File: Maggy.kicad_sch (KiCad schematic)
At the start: 75 parts, among them CN1 0430450800, CN2 430451000, J1 XY308-2.54-2P, J2 XY308-2.54-2P, J3 XY308-2.54-2P, J4 XY308-2.54-2P, U1 CH224K, U10 INA214AIDCKR, U11 Socket for Teensy 4.1 (2x 1x2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, U12 INA214AIDCKR, U13 INA214AIDCKR, U14 TMAG5170A2DGKR, U15 TMAG5170A2DGKR, U16 TMAG5170A2DGKR, U17 TMAG5170A2DGKR, U18 TMAG5170A2DGKR, U2 A4950ELJTR-T, U3 A4950ELJTR-T, U4 A4950ELJTR-T, U5 A4950ELJTR-T, U6 TLV2372, U7 LM1117S-3.3, U8 LM1117S-5.0, U9 INA214AIDCKR

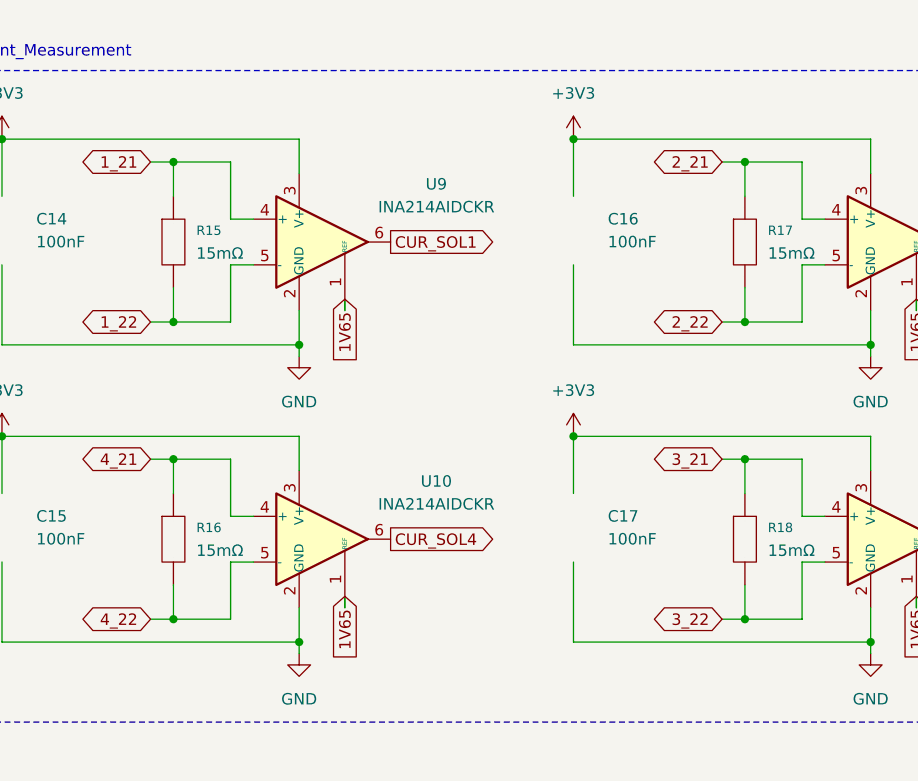
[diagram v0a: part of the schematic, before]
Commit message: chore: replace current sensing resistors' symbols from EasyEDA to KiCad ones
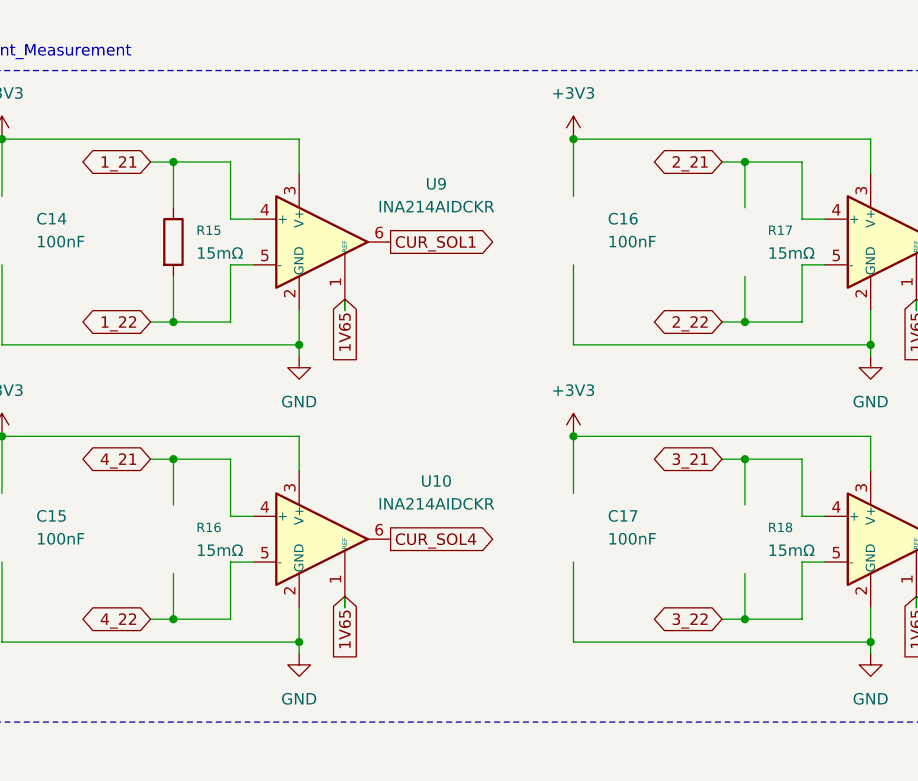
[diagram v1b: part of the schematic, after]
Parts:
- R15, R16, R17, R18: symbol ProPrj_Mag-easyedapro:1206W3F100MT5E -> Device:R
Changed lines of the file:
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@@
 	(wire
 		(pts
+			(xy 224.79 240.03) (xy 224.79 245.11)
+		)
+		(stroke
+			(width 0)
+			(type default)
+		)
+	)
+	(wire
+		(pts
 			(xy 130.81 133.35) (xy 124.46 133.35)
 		)
@@
 	(wire
 		(pts
-			(xy 288.29 241.3) (xy 288.29 245.11)
+			(xy 288.29 240.03) (xy 288.29 245.11)
 		)
 		(stroke
@@
 	(wire
 		(pts
-			(xy 288.29 260.35) (xy 288.29 264.16)
-		)
-		(stroke
-			(width 0)
-			(type default)
-		)
-	)
-	(wire
-		(pts
 			(xy 137.16 121.92) (xy 137.16 124.46)
 		)
@@
 	(wire
 		(pts
-			(xy 224.79 241.3) (xy 224.79 245.11)
-		)
-		(stroke
-			(width 0)
-			(type default)
-		)
-	)
-	(wire
-		(pts
 			(xy 125.73 48.26) (xy 139.7 48.26)
 		)
@@
 	(wire
 		(pts
-			(xy 288.29 274.32) (xy 288.29 278.13)
+			(xy 288.29 273.05) (xy 288.29 278.13)
 		)
 		(stroke
@@
 	(wire
 		(pts
-			(xy 224.79 227.33) (xy 224.79 231.14)
+			(xy 224.79 227.33) (xy 224.79 232.41)
 		)
 		(stroke
@@
 	(wire
 		(pts
-			(xy 288.29 227.33) (xy 288.29 231.14)
+			(xy 288.29 227.33) (xy 288.29 232.41)
 		)
 		(stroke
@@
 	(wire
 		(pts
+			(xy 288.29 260.35) (xy 288.29 265.43)
+		)
+		(stroke
+			(width 0)
+			(type default)
+		)
+	)
+	(wire
+		(pts
 			(xy 78.74 219.71) (xy 85.09 219.71)
 		)
@@
 	(wire
 		(pts
+			(xy 224.79 260.35) (xy 224.79 265.43)
+		)
+		(stroke
+			(width 0)
+			(type default)
+		)
+	)
+	(wire
+		(pts
 			(xy 307.34 243.84) (xy 307.34 242.57)
 		)
@@
 	(wire
 		(pts
-			(xy 224.79 274.32) (xy 224.79 278.13)
+			(xy 224.79 273.05) (xy 224.79 278.13)
 		)
 		(stroke
@@
 	(wire
 		(pts
-			(xy 224.79 260.35) (xy 224.79 264.16)
-		)
-		(stroke
-			(width 0)
-			(type default)
-		)
-	)
-	(wire
-		(pts
 			(xy 85.09 240.03) (xy 85.09 242.57)
 		)
@@
 	)
 	(symbol
-		(lib_id "ProPrj_Mag-easyedapro:1206W3F100MT5E")
-		(at 224.79 269.24 270)
+		(lib_id "Device:R")
+		(at 224.79 269.24 0)
 		(unit 1)
 		(body_style 0)
@@
 		(fields_autoplaced yes)
 		(property "Reference" "R16"
-			(at 227.33 267.97 90)
+			(at 227.33 267.97 0)
 			(show_name no)
 			(do_not_autoplace no)
@@
 		)
 		(property "Value" "15mΩ"
-			(at 227.33 270.5099 90)
+			(at 227.33 270.5099 0)
 			(show_name no)
 			(do_not_autoplace no)
@@
 		)
 		(property "Footprint" "Resistor_SMD:R_1206_3216Metric"
-			(at 224.79 269.24 0)
+			(at 223.012 269.24 90)
 			(hide yes)
 			(show_name no)
@@
 			)
 		)
-		(property "Description" "Type:Thick Film Resistors Resistance:10mΩ Tolerance:±1% Tolerance:±1% Power(Watts): Overload Voltage (Max): Temperature Coefficient:- Temperature Coefficient:- Operating Temperature Range:-55°C~+155°C Operating Temperature Range:-55°C~+155°C"
+		(property "Description" "Resistor"
 			(at 224.79 269.24 0)
 			(hide yes)
@@
 	)
 	(symbol
-		(lib_id "ProPrj_Mag-easyedapro:1206W3F100MT5E")
-		(at 288.29 269.24 270)
+		(lib_id "Device:R")
+		(at 288.29 269.24 0)
 		(unit 1)
 		(body_style 0)
@@
 		(fields_autoplaced yes)
 		(property "Reference" "R18"
-			(at 290.83 267.97 90)
+			(at 290.83 267.97 0)
 			(show_name no)
 			(do_not_autoplace no)
@@
 		)
 		(property "Value" "15mΩ"
-			(at 290.83 270.5099 90)
+			(at 290.83 270.5099 0)
 			(show_name no)
 			(do_not_autoplace no)
@@
 		)
 		(property "Footprint" "Resistor_SMD:R_1206_3216Metric"
-			(at 288.29 269.24 0)
+			(at 286.512 269.24 90)
 			(hide yes)
 			(show_name no)
@@
 			)
 		)
-		(property "Description" "Type:Thick Film Resistors Resistance:10mΩ Tolerance:±1% Tolerance:±1% Power(Watts): Overload Voltage (Max): Temperature Coefficient:- Temperature Coefficient:- Operating Temperature Range:-55°C~+155°C Operating Temperature Range:-55°C~+155°C"
+		(property "Description" "Resistor"
 			(at 288.29 269.24 0)
 			(hide yes)
@@
 	)
 	(symbol
-		(lib_id "ProPrj_Mag-easyedapro:1206W3F100MT5E")
-		(at 224.79 236.22 270)
+		(lib_id "Device:R")
+		(at 224.79 236.22 0)
 		(unit 1)
-		(body_style 0)
+		(body_style 1)
 		(exclude_from_sim no)
 		(in_bom yes)
@@
 		(fields_autoplaced yes)
 		(property "Reference" "R15"
-			(at 227.33 234.95 90)
+			(at 227.33 234.95 0)
 			(show_name no)
 			(do_not_autoplace no)
@@
 		)
 		(property "Value" "15mΩ"
-			(at 227.33 237.4899 90)
+			(at 227.33 237.4899 0)
 			(show_name no)
 			(do_not_autoplace no)
@@
 		)
 		(property "Footprint" "Resistor_SMD:R_1206_3216Metric"
-			(at 224.79 236.22 0)
+			(at 223.012 236.22 90)
 			(hide yes)
 			(show_name no)
@@
 			)
 		)
-		(property "Description" "Type:Thick Film Resistors Resistance:10mΩ Tolerance:±1% Tolerance:±1% Power(Watts): Overload Voltage (Max): Temperature Coefficient:- Temperature Coefficient:- Operating Temperature Range:-55°C~+155°C Operating Temperature Range:-55°C~+155°C"
+		(property "Description" "Resistor"
 			(at 224.79 236.22 0)
 			(hide yes)
@@
 	)
 	(symbol
-		(lib_id "ProPrj_Mag-easyedapro:1206W3F100MT5E")
-		(at 288.29 236.22 270)
+		(lib_id "Device:R")
+		(at 288.29 236.22 0)
 		(unit 1)
 		(body_style 0)
@@
 		(fields_autoplaced yes)
 		(property "Reference" "R17"
-			(at 290.83 234.95 90)
+			(at 290.83 234.95 0)
 			(show_name no)
 			(do_not_autoplace no)
@@
 		)
 		(property "Value" "15mΩ"
-			(at 290.83 237.4899 90)
+			(at 290.83 237.4899 0)
 			(show_name no)
 			(do_not_autoplace no)
@@
 		)
 		(property "Footprint" "Resistor_SMD:R_1206_3216Metric"
-			(at 288.29 236.22 0)
+			(at 286.512 236.22 90)
 			(hide yes)
 			(show_name no)
@@
 			)
 		)
-		(property "Description" "Type:Thick Film Resistors Resistance:10mΩ Tolerance:±1% Tolerance:±1% Power(Watts): Overload Voltage (Max): Temperature Coefficient:- Temperature Coefficient:- Operating Temperature Range:-55°C~+155°C Operating Temperature Range:-55°C~+155°C"
+		(property "Description" "Resistor"
 			(at 288.29 236.22 0)
 			(hide yes)

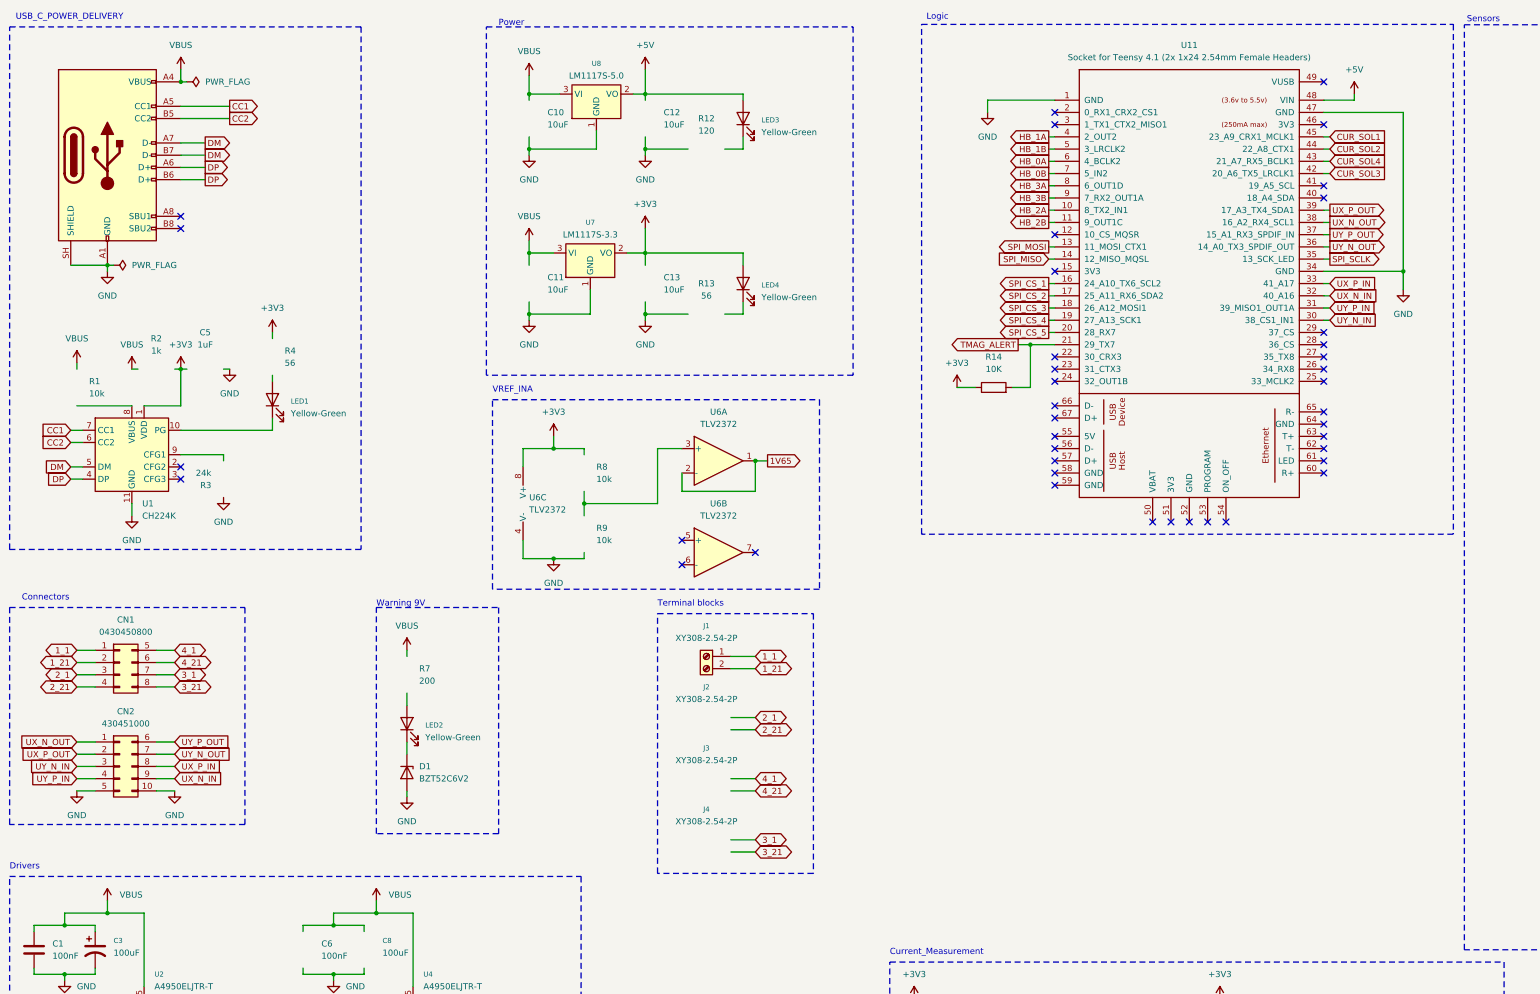
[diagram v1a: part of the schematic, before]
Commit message: chore: add teensy headers to schematic
Added two header rows to the schematic, so they are included on the BOM. These are not to be used for routing, the Teensy is so the pin names and functions are present, but this way the headers should be auto-placed by the manufacturer.

Marked the Teensy as DNP.
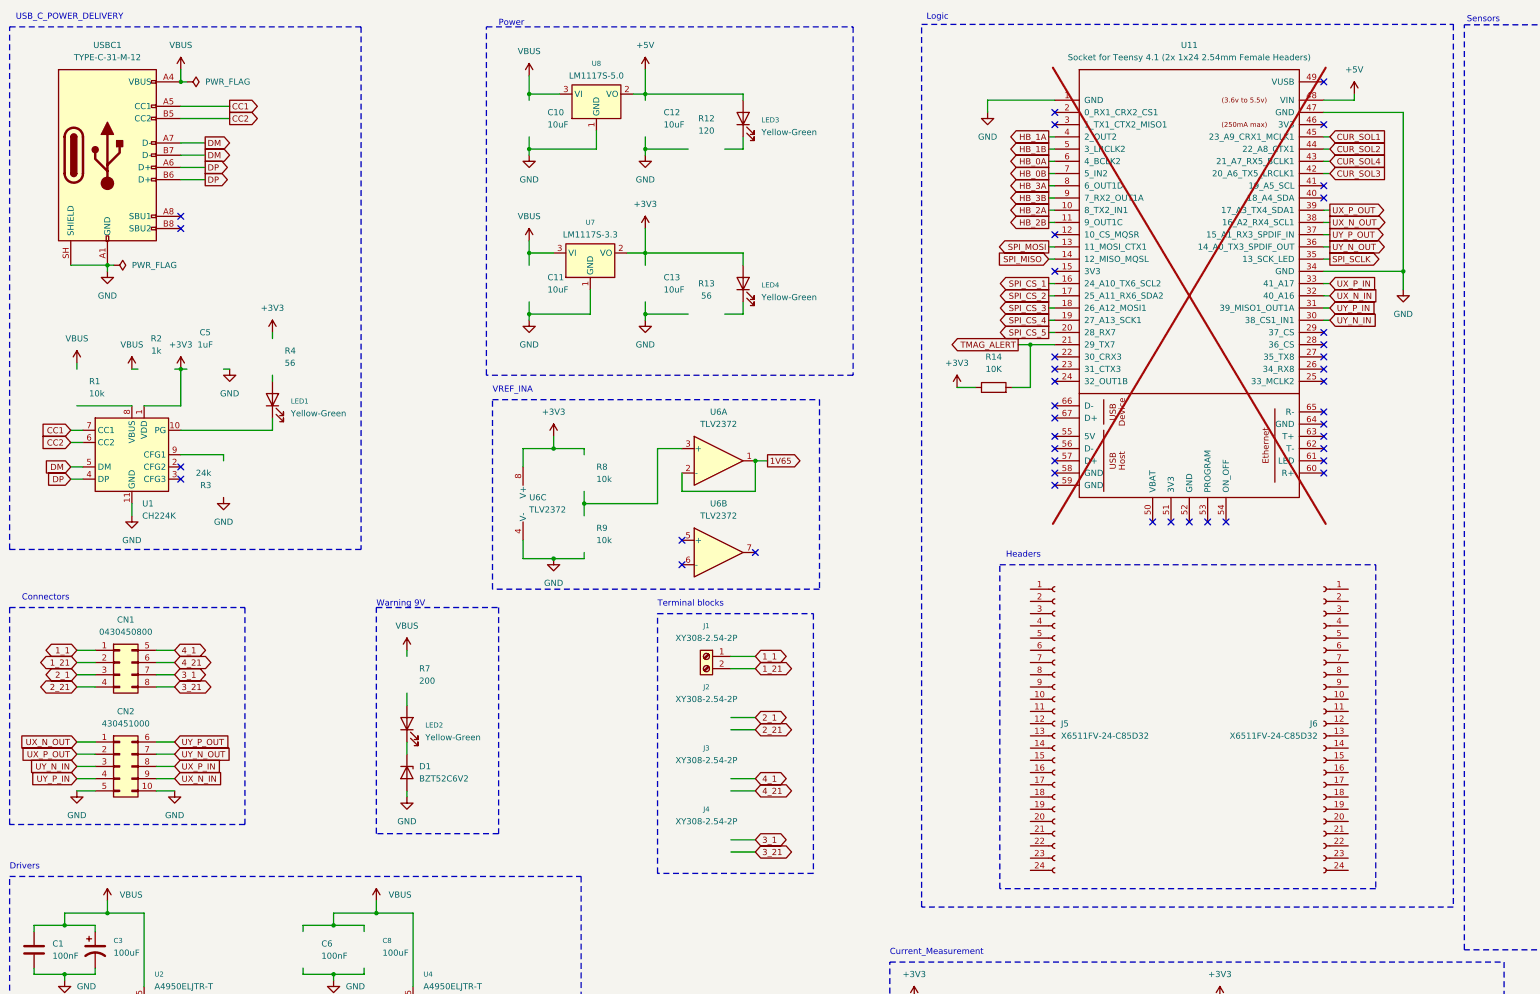
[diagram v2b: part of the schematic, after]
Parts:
- added J5, J6: X6511FV-24-C85D32, Package_DIP:DIP-20_W7.62mm, symbol Connector:Conn_01x24_Socket
- U11: now not fitted
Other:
- note added: "Headers"

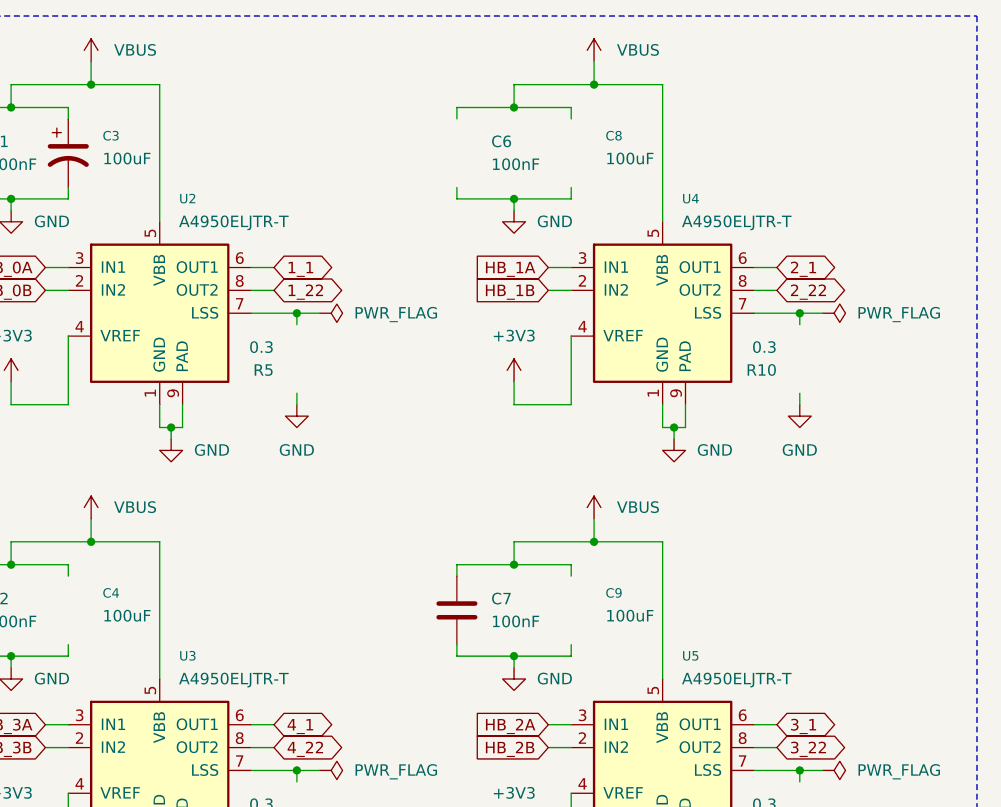
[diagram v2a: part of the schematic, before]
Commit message: fix: motor driver component references
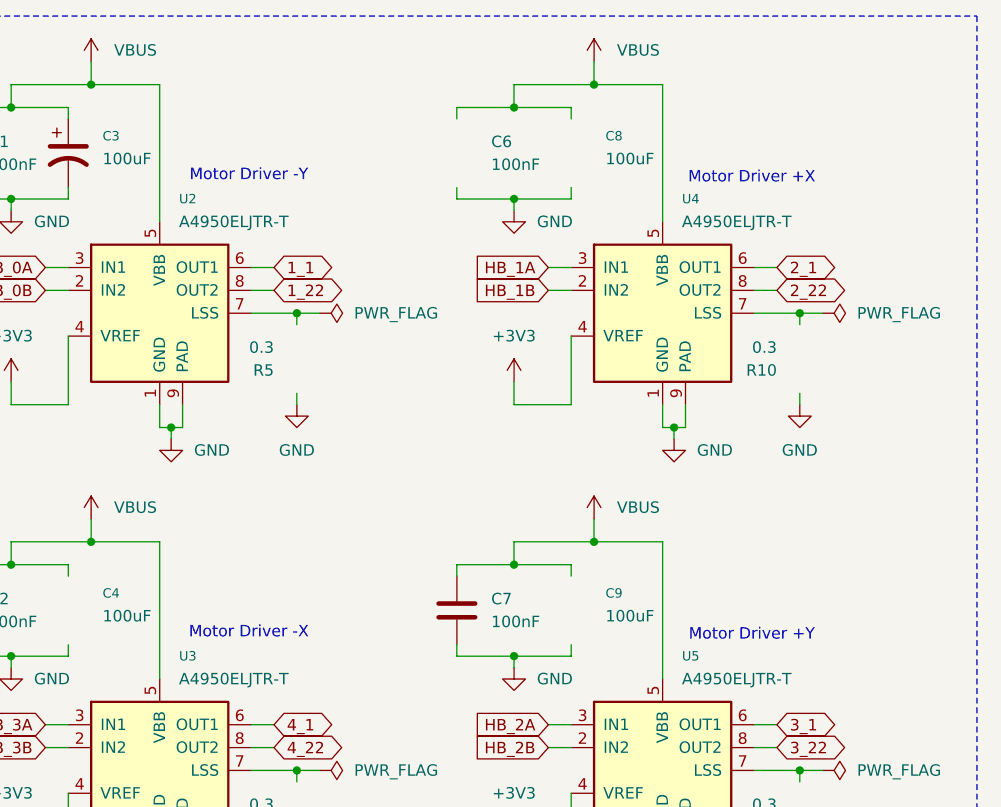
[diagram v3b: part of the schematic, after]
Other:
- note added: "Motor Driver +X"
- note added: "Motor Driver +Y"
- note added: "Motor Driver -X"
- note added: "Motor Driver -Y"
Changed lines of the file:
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@@
+		)
+	)
+	(text "Motor Driver -X\n"
+		(exclude_from_sim no)
+		(at 55.626 267.97 0)
+		(effects
+			(font
+				(size 1.27 1.27)
+			)
 		)
 	)
@@
 		)
 	)
+	(text "Motor Driver +X\n"
+		(exclude_from_sim no)
+		(at 111.506 217.424 0)
+		(effects
+			(font
+				(size 1.27 1.27)
+			)
+		)
+	)
+	(text "Motor Driver -Y"
+		(exclude_from_sim no)
+		(at 55.626 217.17 0)
+		(effects
+			(font
+				(size 1.27 1.27)
+			)
+		)
+	)
 	(text "VREF_INA"
 		(exclude_from_sim no)
@@
 		)
 	)
+	(text "Motor Driver +Y"
+		(exclude_from_sim no)
+		(at 111.506 268.224 0)
+		(effects
+			(font
+				(size 1.27 1.27)
+			)
+		)
+	)

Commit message: fix: current measurement component references
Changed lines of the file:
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@@
+		)
+	)
+	(text "Motor Driver +X\n"
+		(exclude_from_sim no)
+		(at 318.262 227.838 0)
+		(effects
+			(font
+				(size 1.27 1.27)
+			)
 		)
 	)
@@
 		)
 	)
+	(text "Motor Driver +Y"
+		(exclude_from_sim no)
+		(at 318.516 260.604 0)
+		(effects
+			(font
+				(size 1.27 1.27)
+			)
+		)
+	)
 	(text "Headers"
 		(exclude_from_sim no)
@@
 			)
 			(justify left bottom)
+		)
+	)
+	(text "Motor Driver -X\n"
+		(exclude_from_sim no)
+		(at 255.016 260.858 0)
+		(effects
+			(font
+				(size 1.27 1.27)
+			)
 		)
 	)
@@
 		)
 	)
+	(text "Motor Driver -Y"
+		(exclude_from_sim no)
+		(at 254.762 227.584 0)
+		(effects
+			(font
+				(size 1.27 1.27)
+			)
+		)
+	)

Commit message: chore: add teensy footprint to schematic
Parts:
- U11: footprint (none) -> teensy:Teensy41
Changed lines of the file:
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@@
 			)
 		)
-		(property "Footprint" ""
+		(property "Footprint" "teensy:Teensy41"
 			(at 252.73 82.55 0)
 			(hide yes)

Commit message: chore: replaced footprints for linear regulators
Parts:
- U7, U8: footprint Package_TO_SOT_SMD:TO-263-3_TabPin2 -> Package_TO_SOT_SMD:SOT-223-3_TabPin2
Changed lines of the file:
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@@
 			)
 		)
-		(property "Footprint" "Package_TO_SOT_SMD:TO-263-3_TabPin2"
+		(property "Footprint" "Package_TO_SOT_SMD:SOT-223-3_TabPin2"
 			(at 138.43 69.85 0)
 			(hide yes)
@@
 			)
 		)
-		(property "Description" "800mA Low-Dropout Linear Regulator, 3.3V fixed output, TO-263"
+		(property "Description" "800mA Low-Dropout Linear Regulator, 3.3V fixed output, SOT-223"
 			(at 138.43 69.85 0)
 			(hide yes)
@@
 			)
 		)
-		(property "Footprint" "Package_TO_SOT_SMD:TO-263-3_TabPin2"
+		(property "Footprint" "Package_TO_SOT_SMD:SOT-223-3_TabPin2"
 			(at 139.7 36.83 0)
 			(hide yes)
@@
 			)
 		)
-		(property "Description" "800mA Low-Dropout Linear Regulator, 5.0V fixed output, TO-263"
+		(property "Description" "800mA Low-Dropout Linear Regulator, 5.0V fixed output, SOT-223"
 			(at 139.7 36.83 0)
 			(hide yes)

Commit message: chore: updated footprint for VREF op-amp
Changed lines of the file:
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@@
 		(property "Footprint" "Package_SO:SOIC-8_3.9x4.9mm_P1.27mm"
 			(at 165.1 113.03 0)
-			(hide yes)
 			(show_name no)
 			(do_not_autoplace no)
